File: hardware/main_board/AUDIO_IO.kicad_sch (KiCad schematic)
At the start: 10 parts, among them IC501 LM4890M_NOPB, J501 Conn_01x03_Pin, J502 AudioJack

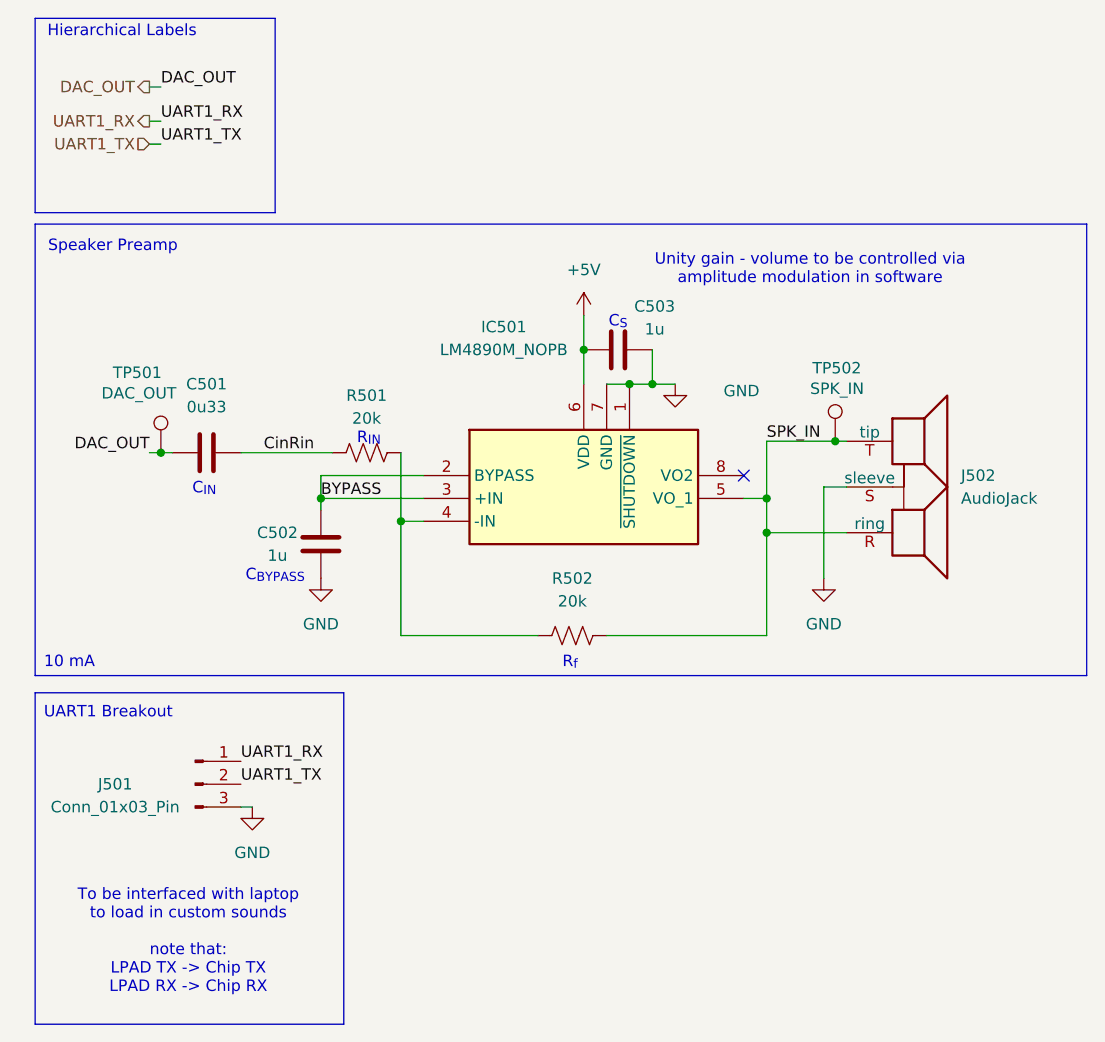
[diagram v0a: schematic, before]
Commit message: changed level shifter. bunch of aesthetic changes. led resistors changed on main board. saving before nuke mouser.co.uk
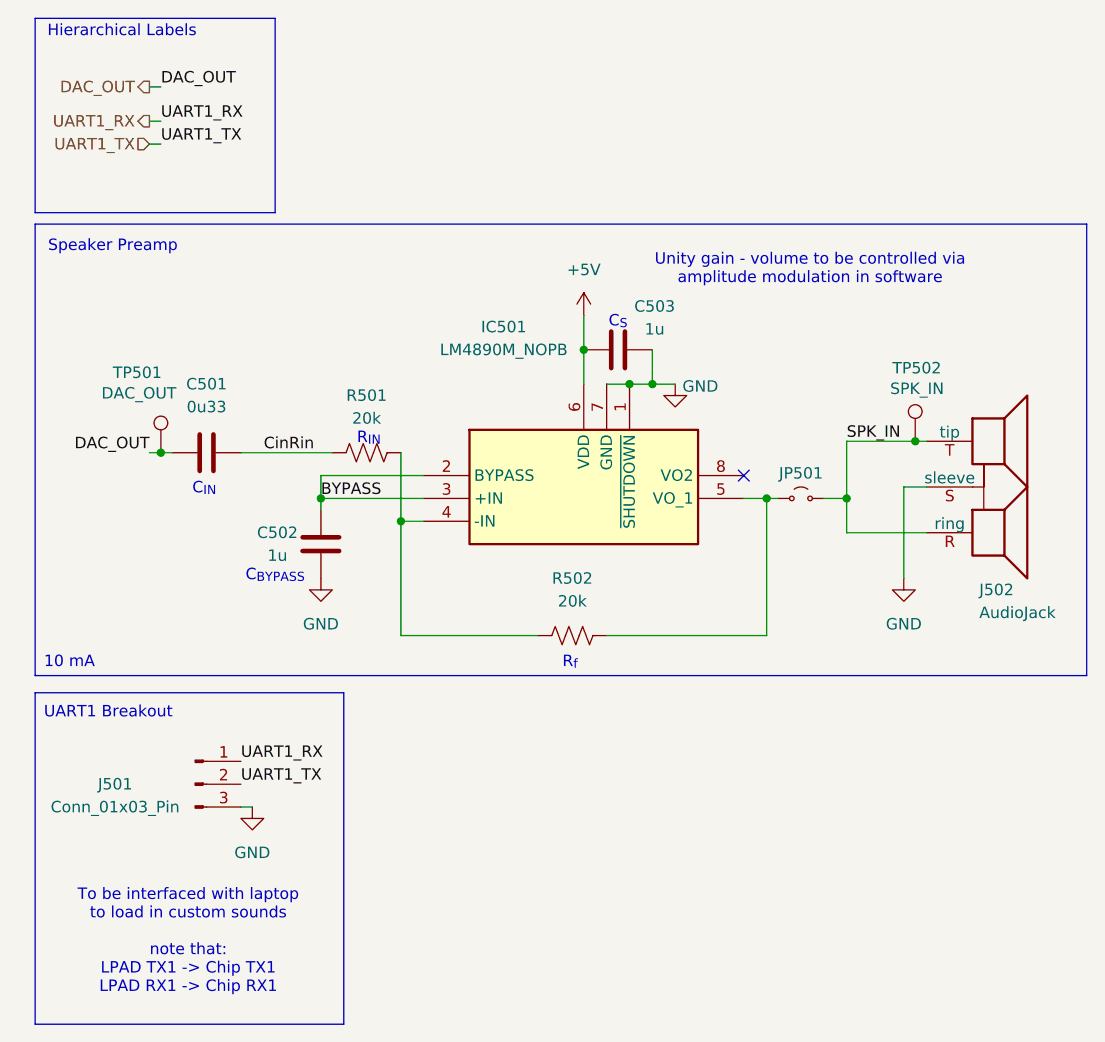
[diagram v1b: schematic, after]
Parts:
- added JP501: Jumper_2_Small_Bridged, Jumper:SolderJumper-2_P1.3mm_Open_TrianglePad1.0x1.5mm, symbol Jumper:Jumper_2_Small_Open
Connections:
- net SPK_IN: now also JP501.2 (B); no longer IC501.5 (VO_1), R502.2
- new net: IC501.5 (VO_1), JP501.1 (A), R502.2
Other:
- note added: "To be interfaced with laptop to load in custom sounds note that: LPAD TX1 -> Chip TX1 LPAD RX1 -> Chip RX1"
- note removed: "To be interfaced with laptop to load in custom sounds note that: LPAD TX -> Chip TX LPAD RX -> Chip RX"
- moved on the sheet: J502, TP502
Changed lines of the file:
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@@
 		)
 	)
-	(text "To be interfaced with laptop\nto load in custom sounds\n\nnote that: \nLPAD TX -> Chip TX\nLPAD RX -> Chip RX"
+	(text "To be interfaced with laptop\nto load in custom sounds\n\nnote that: \nLPAD TX1 -> Chip TX1\nLPAD RX1 -> Chip RX1"
 		(exclude_from_sim no)
 		(at 30.988 116.586 0)
@@
 	)
 	(junction
-		(at 102.87 60.96)
+		(at 111.76 60.96)
 		(diameter 0)
 		(color 0 0 0 0)
@@
 	)
 	(junction
-		(at 95.25 71.12)
+		(at 95.25 67.31)
 		(diameter 0)
 		(color 0 0 0 0)
@@
 	)
 	(junction
-		(at 95.25 67.31)
+		(at 104.14 67.31)
 		(diameter 0)
 		(color 0 0 0 0)
@@
 	(wire
 		(pts
-			(xy 101.6 76.2) (xy 101.6 66.04)
+			(xy 110.49 76.2) (xy 110.49 66.04)
 		)
 		(stroke
@@
 	(wire
 		(pts
+			(xy 92.71 67.31) (xy 95.25 67.31)
+		)
+		(stroke
+			(width 0)
+			(type default)
+		)
+	)
+	(wire
+		(pts
 			(xy 82.55 54.61) (xy 85.09 54.61)
 		)
@@
 	(wire
 		(pts
-			(xy 95.25 71.12) (xy 104.14 71.12)
+			(xy 104.14 71.12) (xy 113.03 71.12)
 		)
 		(stroke
@@
 	(wire
 		(pts
-			(xy 101.6 66.04) (xy 104.14 66.04)
+			(xy 110.49 66.04) (xy 113.03 66.04)
 		)
 		(stroke
@@
 	(wire
 		(pts
-			(xy 95.25 60.96) (xy 102.87 60.96)
+			(xy 104.14 60.96) (xy 111.76 60.96)
 		)
 		(stroke
@@
 	(wire
 		(pts
-			(xy 104.14 60.96) (xy 102.87 60.96)
-		)
-		(stroke
-			(width 0)
-			(type default)
-		)
-	)
-	(wire
-		(pts
-			(xy 95.25 67.31) (xy 95.25 71.12)
+			(xy 113.03 60.96) (xy 111.76 60.96)
+		)
+		(stroke
+			(width 0)
+			(type default)
+		)
+	)
+	(wire
+		(pts
+			(xy 104.14 67.31) (xy 104.14 71.12)
 		)
 		(stroke
@@
 	(wire
 		(pts
-			(xy 95.25 60.96) (xy 95.25 67.31)
+			(xy 104.14 60.96) (xy 104.14 67.31)
 		)
 		(stroke
@@
 	(wire
 		(pts
+			(xy 101.6 67.31) (xy 104.14 67.31)
+		)
+		(stroke
+			(width 0)
+			(type default)
+		)
+	)
+	(wire
+		(pts
 			(xy 27.94 21.59) (xy 26.67 21.59)
 		)
@@
 	(wire
 		(pts
-			(xy 92.71 67.31) (xy 95.25 67.31)
-		)
-		(stroke
-			(width 0)
-			(type default)
-		)
-	)
-	(wire
-		(pts
 			(xy 95.25 82.55) (xy 77.47 82.55)
 		)
@@
 	(wire
 		(pts
+			(xy 95.25 67.31) (xy 96.52 67.31)
+		)
+		(stroke
+			(width 0)
+			(type default)
+		)
+	)
+	(wire
+		(pts
 			(xy 57.15 64.77) (xy 45.72 64.77)
 		)
@@
 	(wire
 		(pts
-			(xy 95.25 71.12) (xy 95.25 82.55)
+			(xy 95.25 67.31) (xy 95.25 82.55)
 		)
 		(stroke
@@
 	)
 	(label "SPK_IN"
-		(at 95.25 60.96 0)
+		(at 104.14 60.96 0)
 		(effects
 			(font
@@
 			)
 			(justify right)
+		)
+	)
+	(symbol
+		(lib_id "Jumper:Jumper_2_Small_Open")
+		(at 99.06 67.31 0)
+		(unit 1)
+		(exclude_from_sim no)
+		(in_bom no)
+		(on_board yes)
+		(dnp no)
+		(property "Reference" "JP501"
+			(at 99.06 64.516 0)
+			(effects
+				(font
+					(size 1.27 1.27)
+				)
+			)
+		)
+		(property "Value" "Jumper_2_Small_Bridged"
+			(at 99.06 64.77 0)
+			(effects
+				(font
+					(size 1.27 1.27)
+				)
+				(hide yes)
+			)
+		)
+		(property "Footprint" "Jumper:SolderJumper-2_P1.3mm_Open_TrianglePad1.0x1.5mm"
+			(at 99.06 67.31 0)
+			(effects
+				(font
+					(size 1.27 1.27)
+				)
+				(hide yes)
+			)
+		)
+		(property "Datasheet" "~"
+			(at 99.06 67.31 0)
+			(effects
+				(font
+					(size 1.27 1.27)
+				)
+				(hide yes)
+			)
+		)
+		(property "Description" "Jumper, 2-pole, small symbol, bridged"
+			(at 99.06 67.31 0)
+			(effects
+				(font
+					(size 1.27 1.27)
+				)
+				(hide yes)
+			)
+		)
+		(pin "1"
+		)
+		(pin "2"
+		)
+		(instances
+			(project "main_board"
+				(path "/5332464e-0c3a-49d2-8fb5-731d0e42ee15/9623dd3b-8db3-4512-88be-dd962a96388d"
+					(reference "JP501")
+					(unit 1)
+				)
+			)
 		)
 	)
@@
 		)
 		(property "Value" "GND"
-			(at 92.456 55.372 0)
+			(at 87.884 54.864 0)
 			(effects
 				(font
@@
 	(symbol
 		(lib_id "Connector:TestPoint")
-		(at 102.87 60.96 0)
+		(at 111.76 60.96 0)
 		(unit 1)
 		(exclude_from_sim no)
@@
 		(dnp no)
 		(property "Reference" "TP502"
-			(at 100.33 52.832 0)
+			(at 109.22 52.832 0)
 			(effects
 				(font
@@
 		)
 		(property "Value" "SPK_IN"
-			(at 100.076 55.118 0)
+			(at 108.966 55.118 0)
 			(effects
 				(font
@@
 		)
 		(property "Footprint" "SamacSys_Parts:bettertestpoint2"
-			(at 107.95 60.96 0)
+			(at 116.84 60.96 0)
 			(effects
 				(font
@@
 		)
 		(property "Datasheet" "~"
-			(at 107.95 60.96 0)
+			(at 116.84 60.96 0)
 			(effects
 				(font
@@
 		)
 		(property "Description" "test point"
-			(at 102.87 60.96 0)
+			(at 111.76 60.96 0)
 			(effects
 				(font
@@
 		)
 		(property "Mouser Price/Inventory" ""
-			(at 102.87 60.96 0)
+			(at 111.76 60.96 0)
 			(effects
 				(font
@@
 	(symbol
 		(lib_id "ECE445L:HeadphoneJack")
-		(at 111.76 59.69 0)
+		(at 120.65 59.69 0)
 		(unit 1)
 		(exclude_from_sim no)
@@
 		(on_board yes)
 		(dnp no)
-		(fields_autoplaced yes)
 		(property "Reference" "J502"
-			(at 116.84 64.7699 0)
+			(at 118.872 77.47 0)
 			(effects
 				(font
@@
 		)
 		(property "Value" "AudioJack"
-			(at 116.84 67.3099 0)
+			(at 118.872 80.01 0)
 			(effects
 				(font
@@
 		)
 		(property "Footprint" "445L:Jack_3.5mm_CUI_SJ1-3523N_Horizontal"
-			(at 109.22 77.47 0)
+			(at 118.11 77.47 0)
 			(effects
 				(font
@@
 		)
 		(property "Datasheet" "~"
-			(at 111.506 60.96 0)
+			(at 120.396 60.96 0)
 			(effects
 				(font
@@
 		)
 		(property "Description" "Speaker"
-			(at 111.76 59.69 0)
+			(at 120.65 59.69 0)
 			(effects
 				(font
@@
 	(symbol
 		(lib_id "power:GND")
-		(at 101.6 76.2 0)
+		(at 110.49 76.2 0)
 		(unit 1)
 		(exclude_from_sim no)
@@
 		(fields_autoplaced yes)
 		(property "Reference" "#PWR0506"
-			(at 101.6 82.55 0)
+			(at 110.49 82.55 0)
 			(effects
 				(font
@@
 		)
 		(property "Value" "GND"
-			(at 101.6 81.28 0)
+			(at 110.49 81.28 0)
 			(effects
 				(font
@@
 		)
 		(property "Footprint" ""
-			(at 101.6 76.2 0)
+			(at 110.49 76.2 0)
 			(effects
 				(font
@@
 		)
 		(property "Datasheet" ""
-			(at 101.6 76.2 0)
+			(at 110.49 76.2 0)
 			(effects
 				(font
@@
 		)
 		(property "Description" "Power symbol creates a global label with name \"GND\" , ground"
-			(at 101.6 76.2 0)
-			(effects
-				(font
+			(at 110.49 76.2 0)
+			(effects
+				(font

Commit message: finished everything except bom information. drc verification
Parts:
- IC501: Mouser Price/Stock https://www.mouser.co.uk/ProductDetail/Texas-Instruments/LM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 -> https://www.mouser.com/ProductDetail/Texas-Instruments/LM48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
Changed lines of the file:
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@@
 			)
 		)
-		(property "Mouser Price/Stock" "https://www.mouser.co.uk/ProductDetail/Texas-Instruments/LM4890M-NOPB?qs=QbsRYf82W3H2uo8qVqZ%252BRw%3D%3D"
+		(property "Mouser Price/Stock" "https://www.mouser.com/ProductDetail/Texas-Instruments/LM4890M-NOPB?qs=QbsRYf82W3H2uo8qVqZ%252BRw%3D%3D"
 			(at 88.9 657.15 0)
 			(effects
